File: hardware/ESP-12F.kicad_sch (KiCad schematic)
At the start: 31 parts, among them J10 PROG_PORT, U10 ESP-12F, U11 MCP2558FD-xMF, U8 PI4IOE5V6416LEX, U9 PI4IOE5V6416LEX

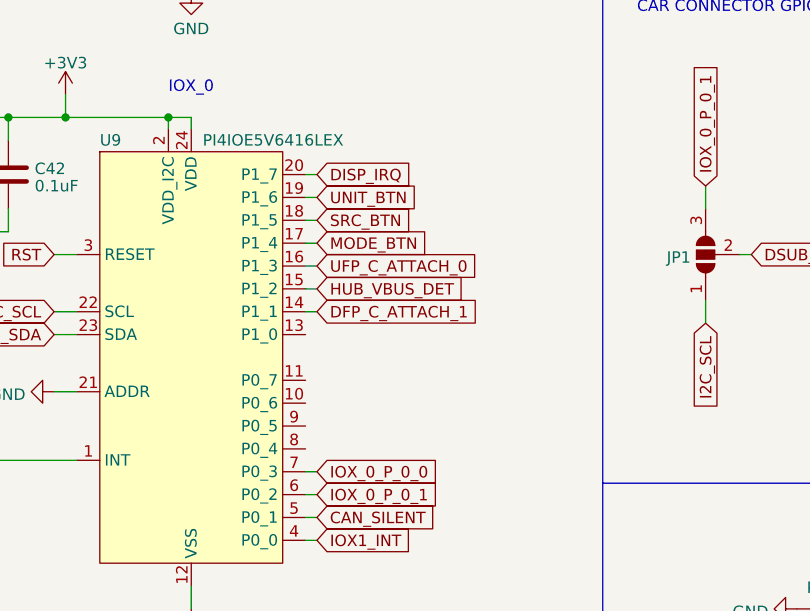
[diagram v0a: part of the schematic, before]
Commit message: worked on usb port and display routing
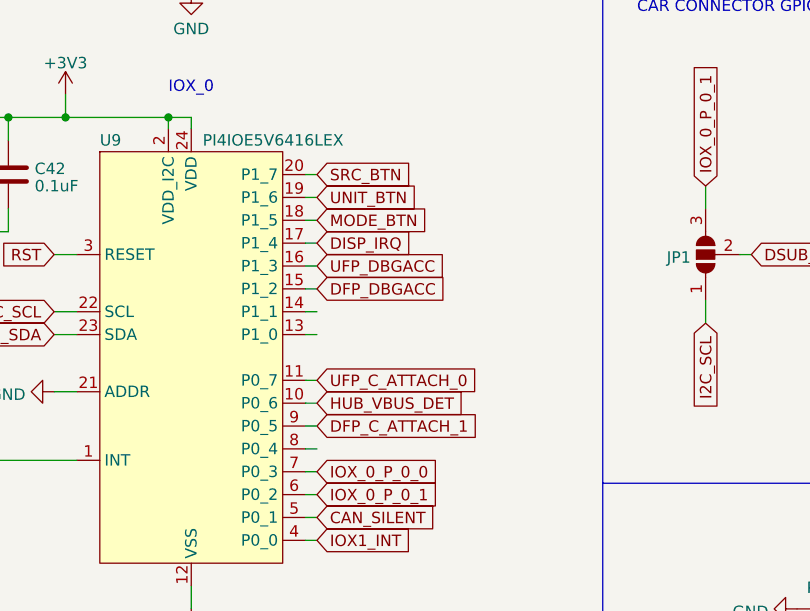
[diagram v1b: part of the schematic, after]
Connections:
- net DFP_C_ATTACH_1: now also U9.9 (P0_5); no longer U9.14 (P1_1)
- net DISP_IRQ: now also U9.17 (P1_4); no longer U9.20 (P1_7)
- net HUB_VBUS_DET: now also U9.10 (P0_6); no longer U9.15 (P1_2)
- net MODE_BTN: now also U9.18 (P1_5); no longer U9.17 (P1_4)
- net SRC_BTN: now also U9.20 (P1_7); no longer U9.18 (P1_5)
- net UFP_C_ATTACH_0: now also U9.11 (P0_7); no longer U9.16 (P1_3)
- new net DFP_DBGACC: U9.15 (P1_2)
- new net UFP_DBGACC: U9.16 (P1_3)
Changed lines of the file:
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@@
+    (stroke (width 0) (type default))
+  )
+  (wire (pts (xy 82.55 149.86) (xy 83.82 149.86))
     (stroke (width 0) (type default))
   )
@@
     (stroke (width 0) (type default))
   )
+  (wire (pts (xy 82.55 144.78) (xy 83.82 144.78))
+    (stroke (width 0) (type default))
+  )
   (wire (pts (xy 49.53 43.18) (xy 38.1 43.18))
     (stroke (width 0) (type default))
@@
     (stroke (width 0) (type default))
   )
+  (wire (pts (xy 82.55 142.24) (xy 83.82 142.24))
+    (stroke (width 0) (type default))
+  )
   (wire (pts (xy 38.1 113.03) (xy 49.53 113.03))
     (stroke (width 0) (type default))
@@
     (stroke (width 0) (type default))
   )
+  (wire (pts (xy 82.55 137.16) (xy 83.82 137.16))
+    (stroke (width 0) (type default))
+  )
   (wire (pts (xy 82.55 124.46) (xy 83.82 124.46))
     (stroke (width 0) (type default))
@@
   )
   (wire (pts (xy 57.15 40.64) (xy 57.15 43.18))
+    (stroke (width 0) (type default))
+  )
+  (wire (pts (xy 82.55 147.32) (xy 83.82 147.32))
     (stroke (width 0) (type default))
   )
@@
     )
   )
-  (global_label "UFP_C_ATTACH_0" (shape input) (at 83.82 129.54 0) (fields_autoplaced)
-    (effects (font (size 1.27 1.27)) (justify left))
-    (property "Intersheetrefs" "${INTERSHEET_REFS}" (at 102.5101 129.54 0)
+  (global_label "UFP_C_ATTACH_0" (shape input) (at 83.82 142.24 0) (fields_autoplaced)
+    (effects (font (size 1.27 1.27)) (justify left))
+    (property "Intersheetrefs" "${INTERSHEET_REFS}" (at 102.5101 142.24 0)
       (effects (font (size 1.27 1.27)) (justify left) hide)
     )
@@
     )
   )
-  (global_label "MODE_BTN" (shape input) (at 83.82 127 0) (fields_autoplaced)
-    (effects (font (size 1.27 1.27)) (justify left))
-    (property "Intersheetrefs" "${INTERSHEET_REFS}" (at 96.4624 127 0)
+  (global_label "MODE_BTN" (shape input) (at 83.82 124.46 0) (fields_autoplaced)
+    (effects (font (size 1.27 1.27)) (justify left))
+    (property "Intersheetrefs" "${INTERSHEET_REFS}" (at 96.4624 124.46 0)
       (effects (font (size 1.27 1.27)) (justify left) hide)
     )
@@
     )
   )
-  (global_label "SRC_BTN" (shape input) (at 83.82 124.46 0) (fields_autoplaced)
-    (effects (font (size 1.27 1.27)) (justify left))
-    (property "Intersheetrefs" "${INTERSHEET_REFS}" (at 95.011 124.46 0)
+  (global_label "SRC_BTN" (shape input) (at 83.82 119.38 0) (fields_autoplaced)
+    (effects (font (size 1.27 1.27)) (justify left))
+    (property "Intersheetrefs" "${INTERSHEET_REFS}" (at 95.011 119.38 0)
       (effects (font (size 1.27 1.27)) (justify left) hide)
     )
@@
     )
   )
-  (global_label "HUB_VBUS_DET" (shape input) (at 83.82 132.08 0) (fields_autoplaced)
-    (effects (font (size 1.27 1.27)) (justify left))
-    (property "Intersheetrefs" "${INTERSHEET_REFS}" (at 100.8772 132.08 0)
+  (global_label "HUB_VBUS_DET" (shape input) (at 83.82 144.78 0) (fields_autoplaced)
+    (effects (font (size 1.27 1.27)) (justify left))
+    (property "Intersheetrefs" "${INTERSHEET_REFS}" (at 100.8772 144.78 0)
       (effects (font (size 1.27 1.27)) (justify left) hide)
     )
@@
     )
   )
+  (global_label "UFP_DBGACC" (shape input) (at 83.82 129.54 0) (fields_autoplaced)
+    (effects (font (size 1.27 1.27)) (justify left))
+    (property "Intersheetrefs" "${INTERSHEET_REFS}" (at 98.8211 129.54 0)
+      (effects (font (size 1.27 1.27)) (justify left) hide)
+    )
+  )
   (global_label "IOX_0_P_0_0" (shape input) (at 83.82 152.4 0) (fields_autoplaced)
     (effects (font (size 1.27 1.27)) (justify left))
@@
     )
   )
+  (global_label "DFP_DBGACC" (shape input) (at 83.82 132.08 0) (fields_autoplaced)
+    (effects (font (size 1.27 1.27)) (justify left))
+    (property "Intersheetrefs" "${INTERSHEET_REFS}" (at 98.7606 132.08 0)
+      (effects (font (size 1.27 1.27)) (justify left) hide)
+    )
+  )
   (global_label "CAN_SILENT" (shape input) (at 83.82 157.48 0) (fields_autoplaced)
     (effects (font (size 1.27 1.27)) (justify left))
@@
     )
   )
-  (global_label "DFP_C_ATTACH_1" (shape input) (at 83.82 134.62 0) (fields_autoplaced)
-    (effects (font (size 1.27 1.27)) (justify left))
-    (property "Intersheetrefs" "${INTERSHEET_REFS}" (at 102.4496 134.62 0)
-      (effects (font (size 1.27 1.27)) (justify left) hide)
-    )
-  )
-  (global_label "DISP_IRQ" (shape input) (at 83.82 119.38 0) (fields_autoplaced)
-    (effects (font (size 1.27 1.27)) (justify left))
-    (property "Intersheetrefs" "${INTERSHEET_REFS}" (at 95.253 119.38 0)
-      (effects (font (size 1.27 1.27)) (justify left) hide)
-    )
+  (global_label "DFP_C_ATTACH_1" (shape input) (at 83.82 147.32 0) (fields_autoplaced)
+    (effects (font (size 1.27 1.27)) (justify left))
+    (property "Intersheetrefs" "${INTERSHEET_REFS}" (at 102.4496 147.32 0)
+      (effects (font (size 1.27 1.27)) (justify left) hide)
+    )
+  )
+  (global_label "DISP_IRQ" (shape input) (at 83.82 127 0) (fields_autoplaced)
+    (effects (font (size 1.27 1.27)) (justify left))
+    (property "Intersheetrefs" "${INTERSHEET_REFS}" (at 95.253 127 0)
+      (effects (font (size 1.27 1.27)) (justify left) hide)
+    )

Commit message: finaliseing pcb layout will come back later for a fresh look
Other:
- company: (none) -> MICK MAKE
- title: (none) -> 200W USB PD 3.1 HUB
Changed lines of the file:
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@@
 (kicad_sch (version 20230121) (generator eeschema)
   (paper "A4")
+  (title_block
+    (title "200W USB PD 3.1 HUB")
+    (date "2023-10-03")
+    (rev "A")
+    (company "MICK MAKE")
+    (comment 1 "THIS IS A 2X 100W USB PD SOURCE ")
+    (comment 2 "HUB USB SPEC 3.1")
+    (comment 3 "TOTAL SYSTEM POWER IS ~275w")
+  )
   (junction (at 148.59 60.96) (diameter 0) (color 0 0 0 0)
   )

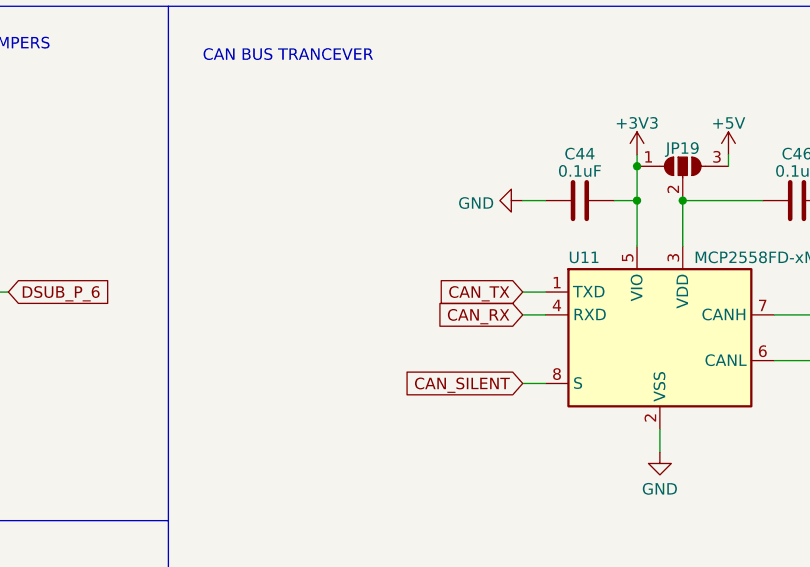
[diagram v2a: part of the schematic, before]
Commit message: working on fixing pcb impeedance
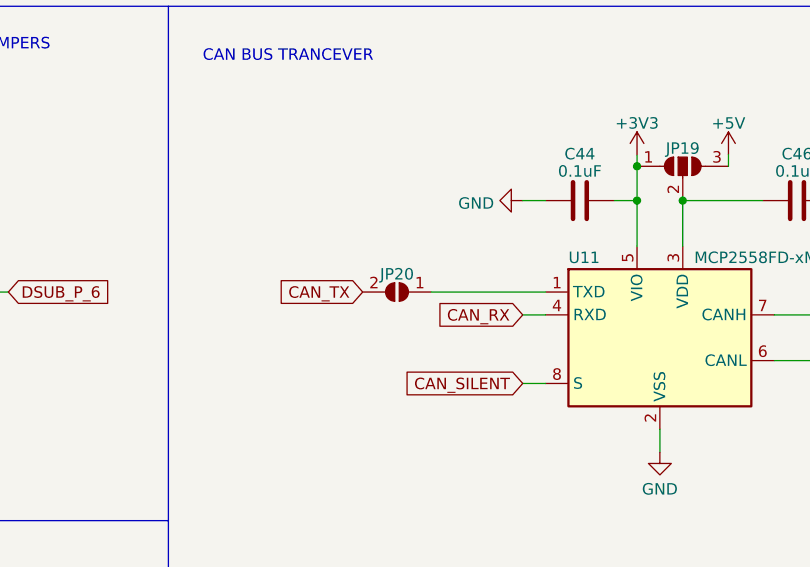
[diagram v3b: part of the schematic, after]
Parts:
- added JP20: ~, Jumper:SolderJumper-2_P1.3mm_Open_RoundedPad1.0x1.5mm, symbol Jumper:SolderJumper_2_Open
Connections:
- net CAN_TX: now also JP20.2 (B); no longer U11.1 (TXD)
- new net: JP20.1 (A), U11.1 (TXD)
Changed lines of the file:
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@@
     (stroke (width 0) (type default))
   )
-  (wire (pts (xy 217.17 128.27) (xy 219.71 128.27))
+  (wire (pts (xy 207.01 128.27) (xy 219.71 128.27))
     (stroke (width 0) (type default))
   )
@@
     )
   )
-  (global_label "CAN_TX" (shape input) (at 217.17 128.27 180) (fields_autoplaced)
-    (effects (font (size 1.27 1.27)) (justify right))
-    (property "Intersheetrefs" "${INTERSHEET_REFS}" (at 207.4304 128.27 0)
+  (global_label "CAN_TX" (shape input) (at 199.39 128.27 180) (fields_autoplaced)
+    (effects (font (size 1.27 1.27)) (justify right))
+    (property "Intersheetrefs" "${INTERSHEET_REFS}" (at 189.6504 128.27 0)
       (effects (font (size 1.27 1.27)) (justify right) hide)
     )
@@
         )
       )
+    )
+  )
+  (symbol (lib_id "Jumper:SolderJumper_2_Open") (at 203.2 128.27 180) (unit 1)
+    (in_bom yes) (on_board yes) (dnp no) (fields_autoplaced)
+    (property "Reference" "JP20" (at 203.2 126.2921 0)
+      (effects (font (size 1.27 1.27)))
+    )
+    (property "Value" "~" (at 204.4773 126.619 90)
+      (effects (font (size 1.27 1.27)) (justify right))
+    )
+    (property "Footprint" "Jumper:SolderJumper-2_P1.3mm_Open_RoundedPad1.0x1.5mm" (at 203.2 128.27 0)
+      (effects (font (size 1.27 1.27)) hide)
+    )
+    (property "Datasheet" "~" (at 203.2 128.27 0)
+      (effects (font (size 1.27 1.27)) hide)
+    )
+    (pin "1")
+    (pin "2")
+    (instances
+      (project "usbc-car-module"
+        (path "/fae025e9-99c5-40c1-af6f-99dc1edbfa43/62352716-6578-44e5-ac45-fc6ae860b12d"
+          (reference "JP20") (unit 1)
+        )
+      )

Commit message: fixed DP issues and finneshed overall routeing
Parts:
- added TP14, TP15, TP16, TP17, TP18: TestPoint, TestPoint:TestPoint_Pad_D1.5mm, symbol Connector:TestPoint
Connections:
- net I2C_SCL: now also TP15.1
- net I2C_SDA: now also TP14.1
- net at U9.13 (P1_0): now also TP17.1
- net at U9.14 (P1_1): now also TP16.1
- net at U9.8 (P0_4): now also TP18.1
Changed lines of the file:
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@@
   (junction (at 148.59 60.96) (diameter 0) (color 0 0 0 0)
   )
+  (junction (at 248.92 60.96) (diameter 0) (color 0 0 0 0)
+  )
   (junction (at 57.15 43.18) (diameter 0) (color 0 0 0 0)
   )
@@
   )
   (junction (at 208.28 33.02) (diameter 0) (color 0 0 0 0)
+  )
+  (junction (at 248.92 63.5) (diameter 0) (color 0 0 0 0)
   )
   (junction (at 201.93 33.02) (diameter 0) (color 0 0 0 0)
@@
     (stroke (width 0) (type default))
   )
-  (wire (pts (xy 217.17 60.96) (xy 265.43 60.96))
+  (wire (pts (xy 217.17 60.96) (xy 248.92 60.96))
     (stroke (width 0) (type default))
   )
@@
     (stroke (width 0) (type default))
   )
+  (wire (pts (xy 248.92 60.96) (xy 265.43 60.96))
+    (stroke (width 0) (type default))
+  )
   (wire (pts (xy 127 133.35) (xy 127 135.89))
     (stroke (width 0) (type default))
   )
-  (wire (pts (xy 82.55 149.86) (xy 83.82 149.86))
+  (wire (pts (xy 82.55 149.86) (xy 100.33 149.86))
     (stroke (width 0) (type default))
   )
@@
     (stroke (width 0) (type default))
   )
-  (wire (pts (xy 82.55 137.16) (xy 83.82 137.16))
+  (wire (pts (xy 82.55 137.16) (xy 100.33 137.16))
     (stroke (width 0) (type default))
   )
@@
     (stroke (width 0) (type default))
   )
-  (wire (pts (xy 217.17 63.5) (xy 273.05 63.5))
+  (wire (pts (xy 217.17 63.5) (xy 248.92 63.5))
     (stroke (width 0) (type default))
   )
@@
     (stroke (width 0) (type default))
   )
+  (wire (pts (xy 248.92 63.5) (xy 273.05 63.5))
+    (stroke (width 0) (type default))
+  )
   (wire (pts (xy 67.31 43.18) (xy 67.31 45.72))
     (stroke (width 0) (type default))
@@
     (stroke (width 0) (type default))
   )
-  (wire (pts (xy 82.55 134.62) (xy 83.82 134.62))
+  (wire (pts (xy 82.55 134.62) (xy 100.33 134.62))
     (stroke (width 0) (type default))
   )
@@
     )
   )
+  (symbol (lib_id "Connector:TestPoint") (at 248.92 60.96 0) (unit 1)
+    (in_bom yes) (on_board yes) (dnp no) (fields_autoplaced)
+    (property "Reference" "TP14" (at 250.317 56.4459 0)
+      (effects (font (size 1.27 1.27)) (justify left))
+    )
+    (property "Value" "TestPoint" (at 250.317 58.8701 0)
+      (effects (font (size 1.27 1.27)) (justify left))
+    )
+    (property "Footprint" "TestPoint:TestPoint_Pad_D1.5mm" (at 254 60.96 0)
+      (effects (font (size 1.27 1.27)) hide)
+    )
+    (property "Datasheet" "~" (at 254 60.96 0)
+      (effects (font (size 1.27 1.27)) hide)
+    )
+    (pin "1")
+    (instances
+      (project "usbc-car-module"
+        (path "/fae025e9-99c5-40c1-af6f-99dc1edbfa43/62352716-6578-44e5-ac45-fc6ae860b12d"
+          (reference "TP14") (unit 1)
+        )
+      )
+    )
+  )
   (symbol (lib_id "power:+3V3") (at 57.15 40.64 0) (unit 1)
     (in_bom yes) (on_board yes) (dnp no) (fields_autoplaced)
@@
         (path "/fae025e9-99c5-40c1-af6f-99dc1edbfa43/62352716-6578-44e5-ac45-fc6ae860b12d"
           (reference "#PWR049") (unit 1)
+        )
+      )
+    )
+  )
+  (symbol (lib_id "Connector:TestPoint") (at 100.33 137.16 270) (unit 1)
+    (in_bom yes) (on_board yes) (dnp no) (fields_autoplaced)
+    (property "Reference" "TP17" (at 105.029 135.9479 90)
+      (effects (font (size 1.27 1.27)) (justify left))
+    )
+    (property "Value" "TestPoint" (at 105.029 138.3721 90)
+      (effects (font (size 1.27 1.27)) (justify left))
+    )
+    (property "Footprint" "TestPoint:TestPoint_Pad_D1.5mm" (at 100.33 142.24 0)
+      (effects (font (size 1.27 1.27)) hide)
+    )
+    (property "Datasheet" "~" (at 100.33 142.24 0)
+      (effects (font (size 1.27 1.27)) hide)
+    )
+    (pin "1")
+    (instances
+      (project "usbc-car-module"
+        (path "/fae025e9-99c5-40c1-af6f-99dc1edbfa43/62352716-6578-44e5-ac45-fc6ae860b12d"
+          (reference "TP17") (unit 1)
         )
       )
@@
     )
   )
+  (symbol (lib_id "Connector:TestPoint") (at 100.33 149.86 270) (unit 1)
+    (in_bom yes) (on_board yes) (dnp no) (fields_autoplaced)
+    (property "Reference" "TP18" (at 105.029 148.6479 90)
+      (effects (font (size 1.27 1.27)) (justify left))
+    )
+    (property "Value" "TestPoint" (at 105.029 151.0721 90)
+      (effects (font (size 1.27 1.27)) (justify left))
+    )
+    (property "Footprint" "TestPoint:TestPoint_Pad_D1.5mm" (at 100.33 154.94 0)
+      (effects (font (size 1.27 1.27)) hide)
+    )
+    (property "Datasheet" "~" (at 100.33 154.94 0)
+      (effects (font (size 1.27 1.27)) hide)
+    )
+    (pin "1")
+    (instances
+      (project "usbc-car-module"
+        (path "/fae025e9-99c5-40c1-af6f-99dc1edbfa43/62352716-6578-44e5-ac45-fc6ae860b12d"
+          (reference "TP18") (unit 1)
+        )
+      )
+    )
+  )
+  (symbol (lib_id "Connector:TestPoint") (at 100.33 134.62 0) (unit 1)
+    (in_bom yes) (on_board yes) (dnp no) (fields_autoplaced)
+    (property "Reference" "TP16" (at 101.727 130.1059 0)
+      (effects (font (size 1.27 1.27)) (justify left))
+    )
+    (property "Value" "TestPoint" (at 101.727 132.5301 0)
+      (effects (font (size 1.27 1.27)) (justify left))
+    )
+    (property "Footprint" "TestPoint:TestPoint_Pad_D1.5mm" (at 105.41 134.62 0)
+      (effects (font (size 1.27 1.27)) hide)
+    )
+    (property "Datasheet" "~" (at 105.41 134.62 0)
+      (effects (font (size 1.27 1.27)) hide)
+    )
+    (pin "1")
+    (instances
+      (project "usbc-car-module"
+        (path "/fae025e9-99c5-40c1-af6f-99dc1edbfa43/62352716-6578-44e5-ac45-fc6ae860b12d"
+          (reference "TP16") (unit 1)
+        )
+      )
+    )
+  )
   (symbol (lib_id "Device:R") (at 157.48 39.37 0) (unit 1)
     (in_bom yes) (on_board yes) (dnp no) (fields_autoplaced)
@@
         )
       )
+    )
+  )
+  (symbol (lib_id "Connector:TestPoint") (at 248.92 63.5 180) (unit 1)
+    (in_bom yes) (on_board yes) (dnp no) (fields_autoplaced)
+    (property "Reference" "TP15" (at 250.317 65.5899 0)
+      (effects (font (size 1.27 1.27)) (justify right))
+    )
+    (property "Value" "TestPoint" (at 250.317 68.0141 0)
+      (effects (font (size 1.27 1.27)) (justify right))
+    )
+    (property "Footprint" "TestPoint:TestPoint_Pad_D1.5mm" (at 243.84 63.5 0)
+      (effects (font (size 1.27 1.27)) hide)
+    )
+    (property "Datasheet" "~" (at 243.84 63.5 0)
+      (effects (font (size 1.27 1.27)) hide)
+    )
+    (pin "1")
+    (instances
+      (project "usbc-car-module"
+        (path "/fae025e9-99c5-40c1-af6f-99dc1edbfa43/62352716-6578-44e5-ac45-fc6ae860b12d"
+          (reference "TP15") (unit 1)
+        )
+      )
